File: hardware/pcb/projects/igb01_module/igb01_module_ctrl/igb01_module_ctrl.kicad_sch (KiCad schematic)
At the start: 276 parts, among them J1 ST_JACK_MIDI_OUT, J10 JACK_MAIN_L_OUT, J11 JACK_MAIN_R_OUT, J12 ST_JACK_MIDI_IN, J13 JACK_RST_OUT, J14 JACK_CV_Y_IN, J15 JACK_CV_E_OUT, J16 JACK_CV_F_OUT, J17 JACK_CV_G_OUT, J18 JACK_CV_H_OUT, J19 JACK_RTN_L_IN, J2 JACK_CLK_OUT, J20 JACK_RTN_R_IN, J21 JACK_SND_L_OUT, J22 JACK_SND_R_OUT, J23 JTAG, J24 LEFT_CON, J25 RIGHT_CON, J27 SWD_CON, J28 DISP_CON1, J29 Micro_SD_Card, J3 JACK_CV_X_IN, J30 Conn_01x03, J31 Conn_01x03, J32 Conn_01x03, J33 POWER_CON, J4 JACK_CV_A_OUT, J5 JACK_CV_B_OUT, J6 JACK_CV_C_OUT, J7 JACK_CV_D_OUT, J8 JACK_EXT_L_IN, J9 JACK_EXT_R_IN, SW1 SW_Push_45deg, SW10 SW_Push_45deg, SW11 SW_Push_45deg, SW12 SW_Push_45deg, SW13 SW_Push_45deg, SW14 SW_Push_45deg, SW15 SW_Push_45deg, SW16 SW_Push_45deg, SW17 SW_Push_45deg, SW18 SW_Push_45deg, SW19 SW_Push_45deg, SW2 SW_Push_45deg, SW20 SW_Push_45deg, SW21 SW_Push_45deg, SW22 SW_Push_45deg, SW23 SW_Push_45deg, SW24 SW_Push_45deg, SW25 SW_Push_45deg, SW26 SW_Push_45deg, SW27 SW_Push_45deg, SW28 SW_Push_45deg, SW29 SW_Push_45deg, SW3 SW_Push_45deg, SW30 SW_Push_45deg, SW31 SW_Push_45deg, SW32 SW_Push_45deg, SW33 SW_Push_45deg, SW34 SW_Push_45deg, SW35 SW_Push_45deg, SW36 SW_Push_45deg, SW4 SW_Push_45deg, SW5 SW_Push_45deg, SW6 SW_Push_45deg, SW7 SW_Push_45deg, SW8 SW_Push_45deg, SW9 SW_Push_45deg, U1 TL074, U10 STM32G431RBTx, U11 TL074, U12 R-78B5.0-2.0, U13 LDK320-3.3V, U14 LDK320-3.3V, U15 LM4040DBZ-10, U2 TL074, U3 74AHCT1G125, U4 TLP2361, U5 74AHCT1G125, U6 74AHCT1G125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

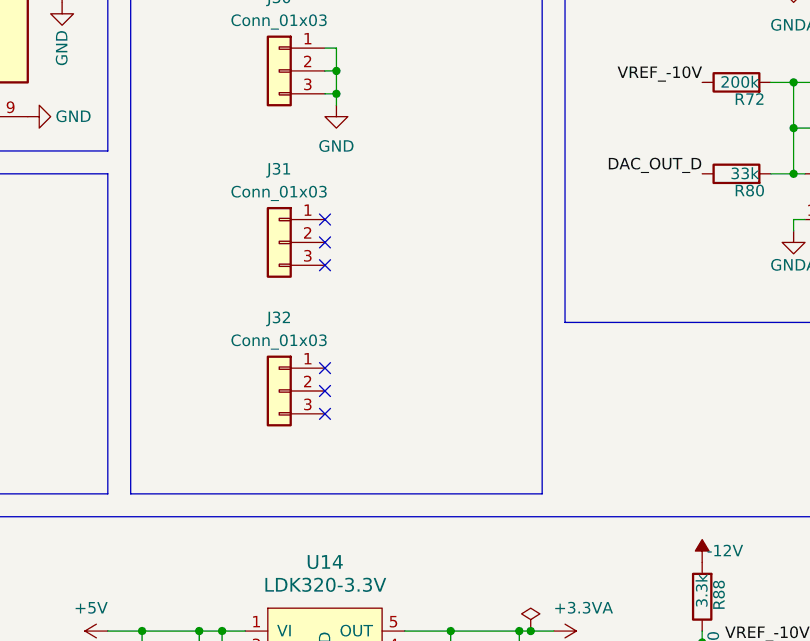
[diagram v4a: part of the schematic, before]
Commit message: add igb01 module led board
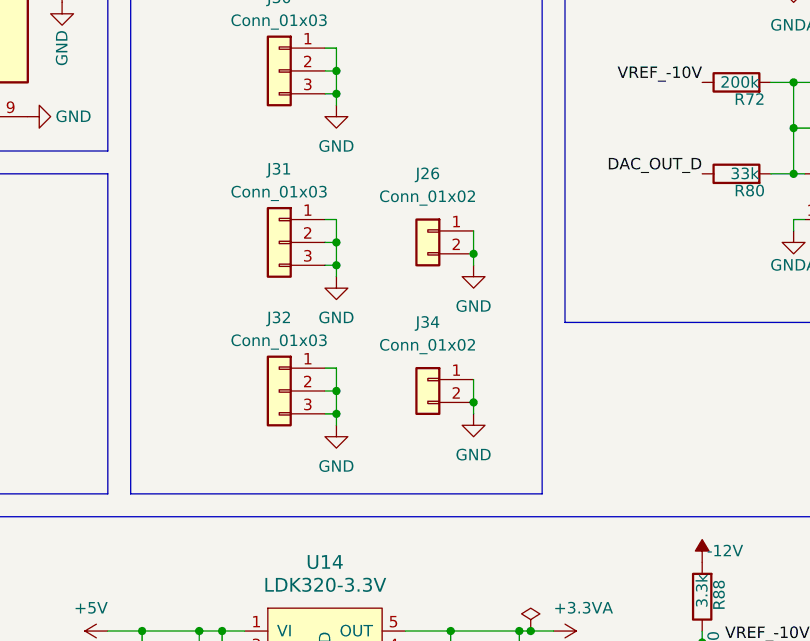
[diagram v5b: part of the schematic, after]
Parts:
- added J26, J34: Conn_01x02, Connector_PinHeader_2.00mm:PinHeader_1x02_P2.00mm_Vertical, symbol Connector_Generic:Conn_01x02
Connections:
- net GND: now also J31.1 (Pin_1), J31.2 (Pin_2), J31.3 (Pin_3), J32.1 (Pin_1), J32.2 (Pin_2), J32.3 (Pin_3), J26.1 (Pin_1), J26.2 (Pin_2), J34.1 (Pin_1), J34.2 (Pin_2)
- no-connect marks 40 -> 34

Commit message: add schematic pdfs
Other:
- title: (none) -> igb01 module ctrl
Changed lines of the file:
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@@
 	(generator_version "9.0")
 	(paper "A2")
+	(title_block
+		(title "igb01 module ctrl")
+		(rev "0.1")
+	)
 	(rectangle
 		(start 113.03 58.42)
